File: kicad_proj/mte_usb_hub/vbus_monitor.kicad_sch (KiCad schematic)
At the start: 1 part

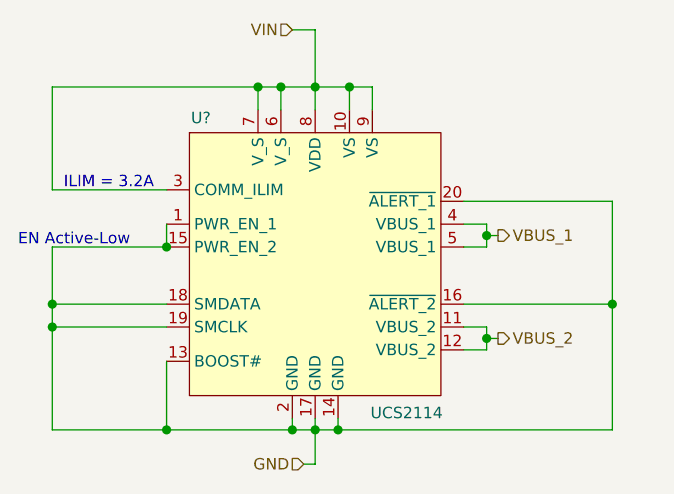
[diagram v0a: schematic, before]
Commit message: Finishes input filter, minor buck changes
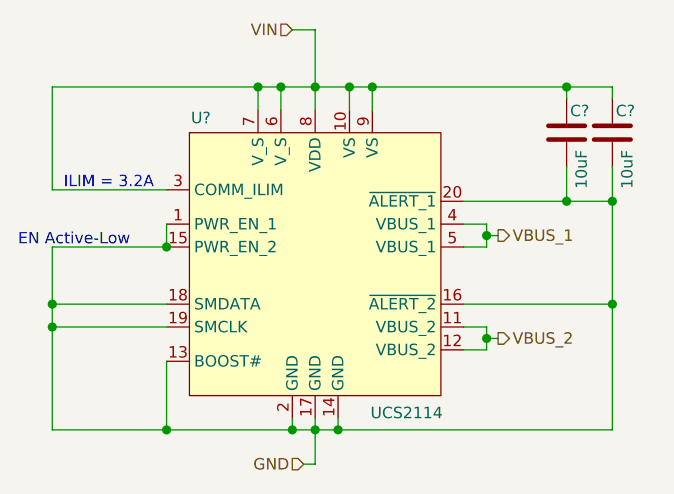
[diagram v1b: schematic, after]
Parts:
- added C? (x2): GRM21BR61H106ME43, footprints:CAPACITOR_0805N, symbol capacitors:GRM21BR61H106ME43
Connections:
- net GND: now also C?.2, C?.2
- net VIN: now also C?.1, C?.1
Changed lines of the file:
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@@
   (junction (at 115.57 95.25) (diameter 1.016) (color 0 0 0 0))
   (junction (at 116.84 57.15) (diameter 1.016) (color 0 0 0 0))
+  (junction (at 119.38 57.15) (diameter 1.016) (color 0 0 0 0))
   (junction (at 132.08 73.66) (diameter 1.016) (color 0 0 0 0))
   (junction (at 132.08 85.09) (diameter 1.016) (color 0 0 0 0))
+  (junction (at 140.97 57.15) (diameter 1.016) (color 0 0 0 0))
+  (junction (at 140.97 69.85) (diameter 1.016) (color 0 0 0 0))
+  (junction (at 146.05 69.85) (diameter 1.016) (color 0 0 0 0))
   (junction (at 146.05 81.28) (diameter 1.016) (color 0 0 0 0))
   (wire (pts (xy 83.82 57.15) (xy 106.68 57.15))
@@
     (stroke (width 0) (type solid) (color 0 0 0 0))
   )
+  (wire (pts (xy 119.38 57.15) (xy 140.97 57.15))
+    (stroke (width 0) (type solid) (color 0 0 0 0))
+  )
   (wire (pts (xy 119.38 59.69) (xy 119.38 57.15))
     (stroke (width 0) (type solid) (color 0 0 0 0))
   )
-  (wire (pts (xy 129.54 69.85) (xy 146.05 69.85))
+  (wire (pts (xy 129.54 69.85) (xy 140.97 69.85))
     (stroke (width 0) (type solid) (color 0 0 0 0))
   )
@@
   )
   (wire (pts (xy 132.08 85.09) (xy 133.35 85.09))
+    (stroke (width 0) (type solid) (color 0 0 0 0))
+  )
+  (wire (pts (xy 140.97 57.15) (xy 140.97 58.42))
+    (stroke (width 0) (type solid) (color 0 0 0 0))
+  )
+  (wire (pts (xy 140.97 57.15) (xy 146.05 57.15))
+    (stroke (width 0) (type solid) (color 0 0 0 0))
+  )
+  (wire (pts (xy 140.97 66.04) (xy 140.97 69.85))
+    (stroke (width 0) (type solid) (color 0 0 0 0))
+  )
+  (wire (pts (xy 140.97 69.85) (xy 146.05 69.85))
+    (stroke (width 0) (type solid) (color 0 0 0 0))
+  )
+  (wire (pts (xy 146.05 58.42) (xy 146.05 57.15))
+    (stroke (width 0) (type solid) (color 0 0 0 0))
+  )
+  (wire (pts (xy 146.05 66.04) (xy 146.05 69.85))
     (stroke (width 0) (type solid) (color 0 0 0 0))
   )
@@
     (effects (font (size 1.27 1.27)) (justify left))
   )
+  (symbol (lib_id "capacitors:GRM21BR61H106ME43") (at 140.97 62.23 0)
+    (in_bom yes) (on_board yes)
+    (property "Reference" "C?" (id 0) (at 141.3511 59.8106 0)
+      (effects (font (size 1.27 1.27)) (justify left))
+    )
+    (property "Value" "GRM21BR61H106ME43" (id 1) (at 141.605 64.77 0)
+      (effects (font (size 1.27 1.27)) (justify left) hide)
+    )
+    (property "Footprint" "footprints:CAPACITOR_0805N" (id 2) (at 141.9352 66.04 0)
+      (effects (font (size 1.27 1.27)) hide)
+    )
+    (property "Datasheet" "" (id 3) (at 140.97 62.23 0)
+      (effects (font (size 1.27 1.27)) hide)
+    )
+    (property "id" "10uF" (id 4) (at 142.6211 68.4593 90)
+      (effects (font (size 1.27 1.27)) (justify left))
+    )
+    (property "manf" "Murata Electronics" (id 5) (at 140.97 62.23 0)
+      (effects (font (size 1.27 1.27)) hide)
+    )
+    (pin "1")
+    (pin "2")
+  )
+  (symbol (lib_id "capacitors:GRM21BR61H106ME43") (at 146.05 62.23 0)
+    (in_bom yes) (on_board yes)
+    (property "Reference" "C?" (id 0) (at 146.4311 59.8106 0)
+      (effects (font (size 1.27 1.27)) (justify left))
+    )
+    (property "Value" "GRM21BR61H106ME43" (id 1) (at 146.685 64.77 0)
+      (effects (font (size 1.27 1.27)) (justify left) hide)
+    )
+    (property "Footprint" "footprints:CAPACITOR_0805N" (id 2) (at 147.0152 66.04 0)
+      (effects (font (size 1.27 1.27)) hide)
+    )
+    (property "Datasheet" "" (id 3) (at 146.05 62.23 0)
+      (effects (font (size 1.27 1.27)) hide)
+    )
+    (property "id" "10uF" (id 4) (at 147.7011 68.4593 90)
+      (effects (font (size 1.27 1.27)) (justify left))
+    )
+    (property "manf" "Murata Electronics" (id 5) (at 146.05 62.23 0)
+      (effects (font (size 1.27 1.27)) hide)
+    )
+    (pin "1")
+    (pin "2")
+  )
   (symbol (lib_name "mte_usb_hub:UCS2114_1") (lib_id "mte_usb_hub:UCS2114") (at 113.03 77.47 0)

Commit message: Updates input protection, output BC enabled
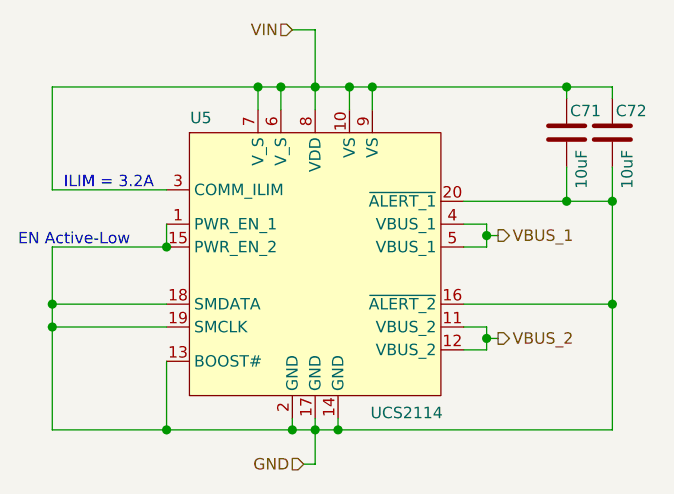
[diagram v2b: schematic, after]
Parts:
- gave numbers to parts that had none: 3
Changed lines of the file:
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@@
-(kicad_sch (version 20210126) (generator eeschema)
+(kicad_sch (version 20210406) (generator eeschema)
   (paper "A4")
   (junction (at 83.82 81.28) (diameter 1.016) (color 0 0 0 0))
@@
   (symbol (lib_id "capacitors:GRM21BR61H106ME43") (at 140.97 62.23 0)
     (in_bom yes) (on_board yes)
-    (property "Reference" "C?" (id 0) (at 141.3511 59.8106 0)
+    (property "Reference" "C71" (id 0) (at 141.3511 59.8106 0)
       (effects (font (size 1.27 1.27)) (justify left))
     )
@@
   (symbol (lib_id "capacitors:GRM21BR61H106ME43") (at 146.05 62.23 0)
     (in_bom yes) (on_board yes)
-    (property "Reference" "C?" (id 0) (at 146.4311 59.8106 0)
+    (property "Reference" "C72" (id 0) (at 146.4311 59.8106 0)
       (effects (font (size 1.27 1.27)) (justify left))
     )
@@
     (pin "2")
   )
-  (symbol (lib_name "mte_usb_hub:UCS2114_1") (lib_id "mte_usb_hub:UCS2114") (at 113.03 77.47 0)
+  (symbol (lib_id "mte_usb_hub:UCS2114") (at 113.03 77.47 0)
     (in_bom yes) (on_board yes)
-    (property "Reference" "U?" (id 0) (at 100.33 60.5854 0))
+    (property "Reference" "U5" (id 0) (at 100.33 60.5854 0))
     (property "Value" "UCS2114" (id 1) (at 123.19 93.3641 0))
     (property "Footprint" "" (id 2) (at 113.03 77.47 0)

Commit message: New changes from the livestream
Starts the layout
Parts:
- C77: renamed from C71; footprint footprints:CAPACITOR_0805N -> mte_usb_footprints:CAPACITOR_0805N
- C78: renamed from C72; footprint footprints:CAPACITOR_0805N -> mte_usb_footprints:CAPACITOR_0805N
- U6: renamed from U5; footprint (none) -> mte_usb_footprints:UCS2114
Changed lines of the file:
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@@
   (symbol (lib_id "capacitors:GRM21BR61H106ME43") (at 140.97 62.23 0)
     (in_bom yes) (on_board yes)
-    (property "Reference" "C71" (id 0) (at 141.3511 59.8106 0)
+    (property "Reference" "C77" (id 0) (at 141.3511 59.8106 0)
       (effects (font (size 1.27 1.27)) (justify left))
     )
@@
       (effects (font (size 1.27 1.27)) (justify left) hide)
     )
-    (property "Footprint" "footprints:CAPACITOR_0805N" (id 2) (at 141.9352 66.04 0)
+    (property "Footprint" "mte_usb_footprints:CAPACITOR_0805N" (id 2) (at 141.9352 66.04 0)
       (effects (font (size 1.27 1.27)) hide)
     )
@@
   (symbol (lib_id "capacitors:GRM21BR61H106ME43") (at 146.05 62.23 0)
     (in_bom yes) (on_board yes)
-    (property "Reference" "C72" (id 0) (at 146.4311 59.8106 0)
+    (property "Reference" "C78" (id 0) (at 146.4311 59.8106 0)
       (effects (font (size 1.27 1.27)) (justify left))
     )
@@
       (effects (font (size 1.27 1.27)) (justify left) hide)
     )
-    (property "Footprint" "footprints:CAPACITOR_0805N" (id 2) (at 147.0152 66.04 0)
+    (property "Footprint" "mte_usb_footprints:CAPACITOR_0805N" (id 2) (at 147.0152 66.04 0)
       (effects (font (size 1.27 1.27)) hide)
     )
@@
   (symbol (lib_id "mte_usb_hub:UCS2114") (at 113.03 77.47 0)
     (in_bom yes) (on_board yes)
-    (property "Reference" "U5" (id 0) (at 100.33 60.5854 0))
+    (property "Reference" "U6" (id 0) (at 100.33 60.5854 0))
     (property "Value" "UCS2114" (id 1) (at 123.19 93.3641 0))
-    (property "Footprint" "" (id 2) (at 113.03 77.47 0)
+    (property "Footprint" "mte_usb_footprints:UCS2114" (id 2) (at 113.03 77.47 0)
       (effects (font (size 1.27 1.27)) hide)
     )

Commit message: Updates from the livestream
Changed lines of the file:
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@@
-(kicad_sch (version 20210406) (generator eeschema)
+(kicad_sch (version 20210606) (generator eeschema)
   (paper "A4")
   (junction (at 83.82 81.28) (diameter 1.016) (color 0 0 0 0))
